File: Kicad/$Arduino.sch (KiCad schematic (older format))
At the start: 1 part

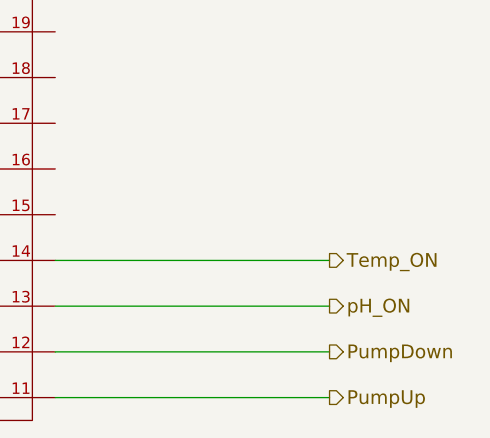
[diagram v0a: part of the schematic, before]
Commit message: changed to mcp3221 - not complete
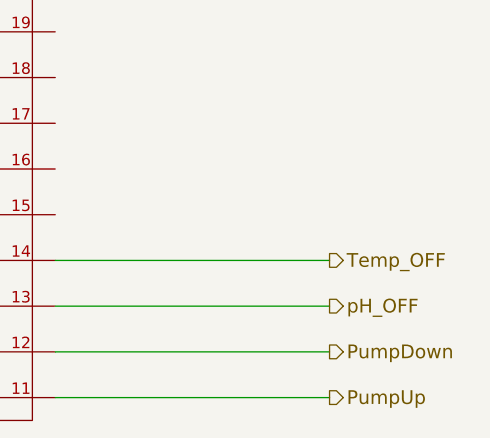
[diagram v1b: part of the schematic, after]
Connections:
- net Temp_ON renamed Temp_OFF
- net pH_ON renamed pH_OFF
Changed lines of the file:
@@
 SCL
 Text HLabel 6950 4200 2    60   Output ~ 0
-pH_ON
+pH_OFF
 Wire Wire Line
 	5750 4200 6950 4200
 Text HLabel 6950 4000 2    60   Output ~ 0
-Temp_ON
+Temp_OFF
 Wire Wire Line
 	5750 4000 6950 4000
